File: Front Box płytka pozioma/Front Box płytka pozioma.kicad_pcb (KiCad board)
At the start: 4 copper layers, 131 x 75 mm, 11 parts, among them J14 Diagnostyka, J15 sockety płytka pozioma, J4 Sygnały, J5 Zasilanie+CAN, J6 Taśma IDC dolna

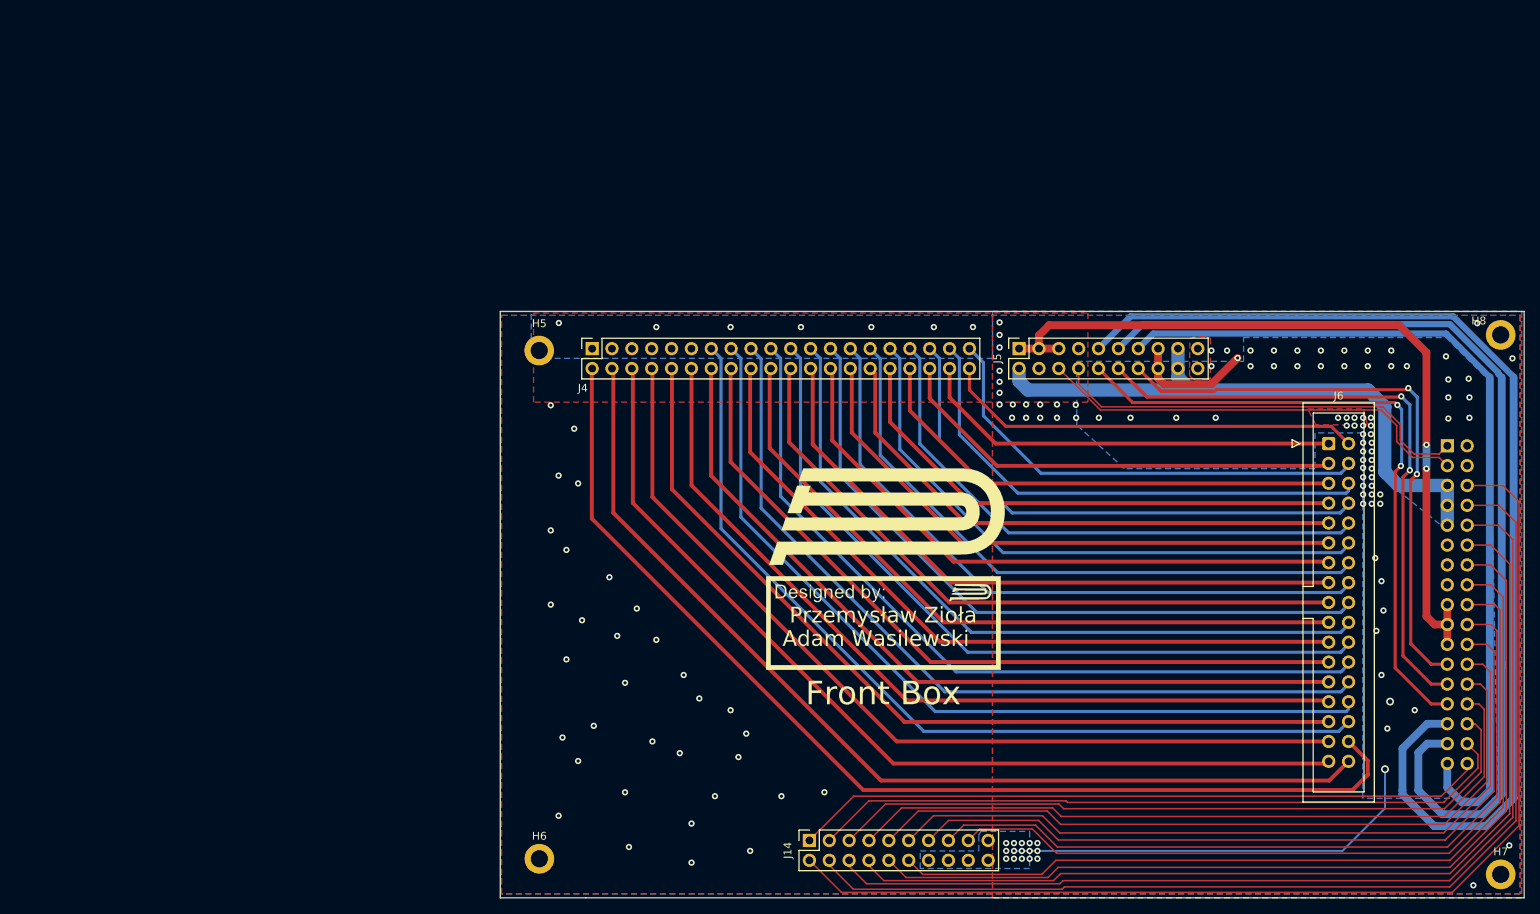
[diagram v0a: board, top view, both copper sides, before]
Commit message: quick revision
Added LED's to horizontal board, distance between sockets fix, Diagnostic Board 5v line delete and compatibility with HDMI fix
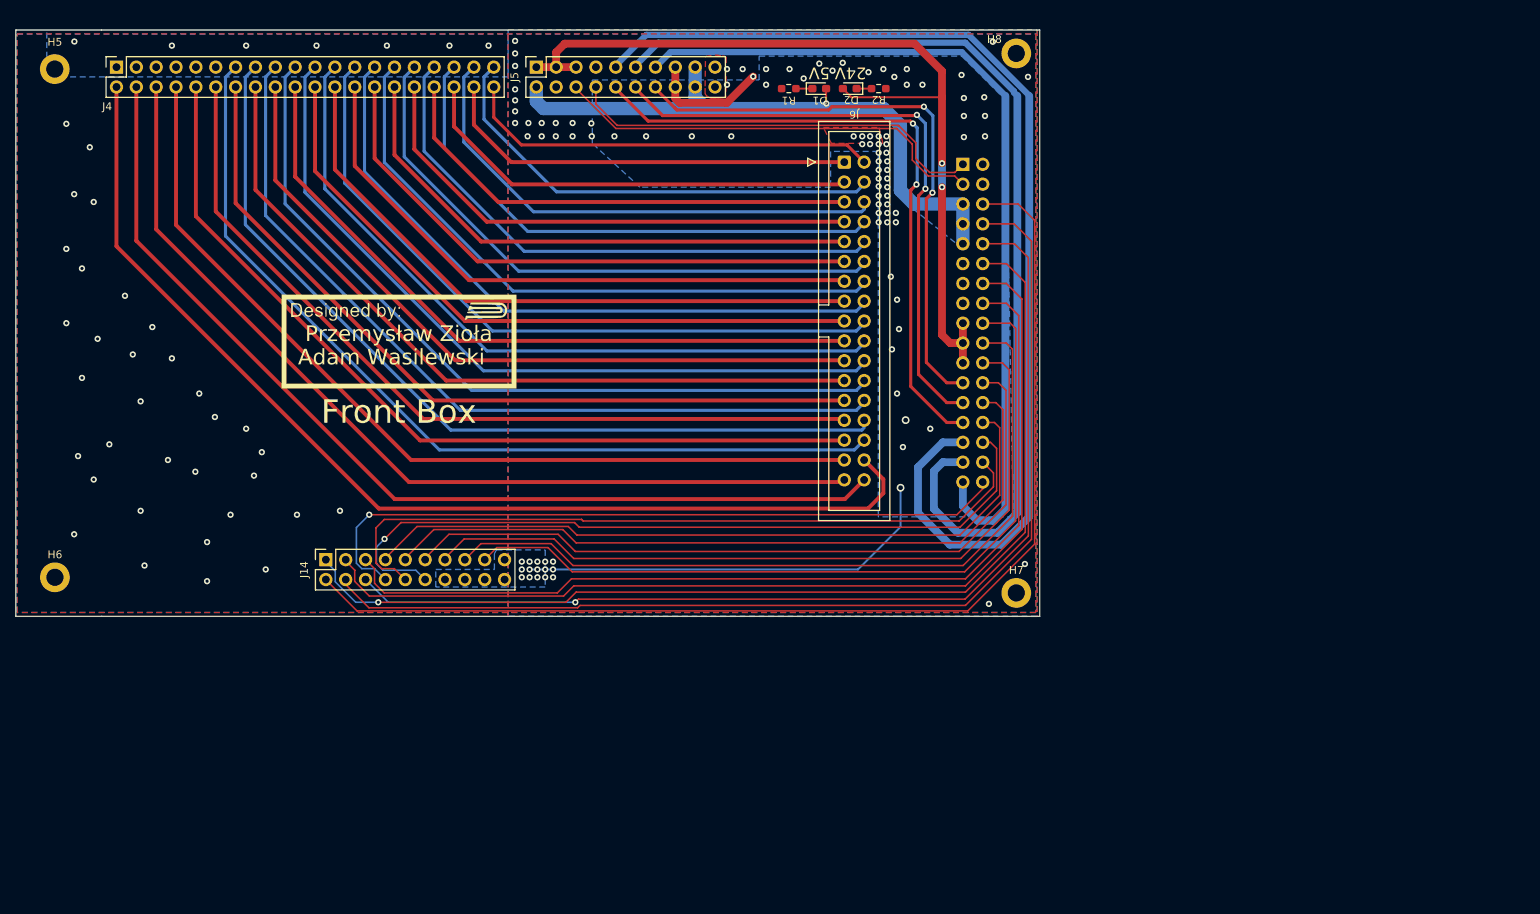
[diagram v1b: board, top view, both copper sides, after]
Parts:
- removed the G*** at (133.5, 87.4)
- added D1: 5v indicator, LED_SMD:LED_0603_1608Metric_Pad1.05x0.95mm_HandSolder, F.Cu at (125.8, 33.0)
- added D2: 24v indicator, LED_SMD:LED_0603_1608Metric_Pad1.05x0.95mm_HandSolder, F.Cu at (129.7, 33.0)
- added R1: 480R, Resistor_SMD:R_0603_1608Metric_Pad0.98x0.95mm_HandSolder, F.Cu at (121.9, 33.0)
- added R2: 480R, Resistor_SMD:R_0603_1608Metric_Pad0.98x0.95mm_HandSolder, F.Cu at (133.4, 33.0)
- moved G*** 71.7 mm to (72.0, 65.3)
- moved H5 71.7 mm to (28.0, 30.5)
- moved H6 71.7 mm to (28.0, 95.5)
- moved H7 71.7 mm to (151.0, 97.5)
- moved H8 71.7 mm to (151.0, 28.5)
- moved J15 71.7 mm to (144.2, 42.7)
- moved J6 71.7 mm to (129.0, 42.4)
- moved J14 71.5 mm to (62.7, 93.2)
- moved J5 71.5 mm to (89.6, 30.2)
- moved J4 70.7 mm to (35.9, 30.2)
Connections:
- J14 pad 1: /SWD1 -> /SWD5
- J14 pad 10: /CLK5 -> /CLK1
- J14 pad 12: /RST5 -> /RST1
- J14 pad 3: /CLK1 -> /CLK5
- J14 pad 5: /RST1 -> /RST5
- J14 pad 8: /SWD5 -> /SWD1
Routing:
- net /+24F2: track 100.9 -> 114.0 mm
- net /RST5: track 112.5 -> 122.1 mm
- net /CLK5: track 118.7 -> 128.2 mm
- net /SWD5: track 125.4 -> 134.8 mm, vias 0 -> 1
- net /RST1: track 92.4 -> 99.5 mm, vias 0 -> 1
- net /CLK1: track 90.7 -> 94.2 mm
- net /SWD1: track 88.7 -> 92.2 mm, vias 0 -> 1
- net Net-(D1-Pad1): track 0.00 -> 2.11 mm
- net Net-(D2-Pad1): track 0.00 -> 1.91 mm
- net +5V: track 77.9 -> 79.6 mm, vias 0 -> 1
- net /TIM_IN0: track 65.2 -> 65.8 mm
- net /S27: track 85.0 -> 85.6 mm
- net /S21: track 97.3 -> 97.9 mm
- net /S19: track 101.8 -> 102.4 mm
- net /K_OUTPUT0: track 76.7 -> 77.3 mm
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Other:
- board text added: "24V"
- board text added: "5V"

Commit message: Changed mounting holes to M3 size because Maciej was crying a lot
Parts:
- removed H5, H6, H7, H8: MountingHole_Pad, MountingHole:MountingHole_2.2mm_M2_DIN965_Pad
- added H1: MountingHole_Pad, MountingHole:MountingHole_3.2mm_M3_DIN965_Pad, F.Cu at (151.0, 97.5)
- added H2: MountingHole_Pad, MountingHole:MountingHole_3.2mm_M3_DIN965_Pad, F.Cu at (28.0, 95.5)
- added H3: MountingHole_Pad, MountingHole:MountingHole_3.2mm_M3_DIN965_Pad, F.Cu at (28.0, 30.5)
- added H4: MountingHole_Pad, MountingHole:MountingHole_3.2mm_M3_DIN965_Pad, F.Cu at (151.0, 28.5)
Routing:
- net /Z13: track 110.6 -> 109.6 mm
- net /Z11: track 128.5 -> 127.7 mm
- net /Z9: track 142.1 -> 141.5 mm
- net /SWD4: track 144.8 -> 145.1 mm, vias 0 -> 2
- net GND: vias 142 -> 146
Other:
- board size 131 x 75 mm -> 131.1 x 75.2 mm
